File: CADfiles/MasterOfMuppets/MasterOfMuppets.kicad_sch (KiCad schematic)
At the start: 0 parts

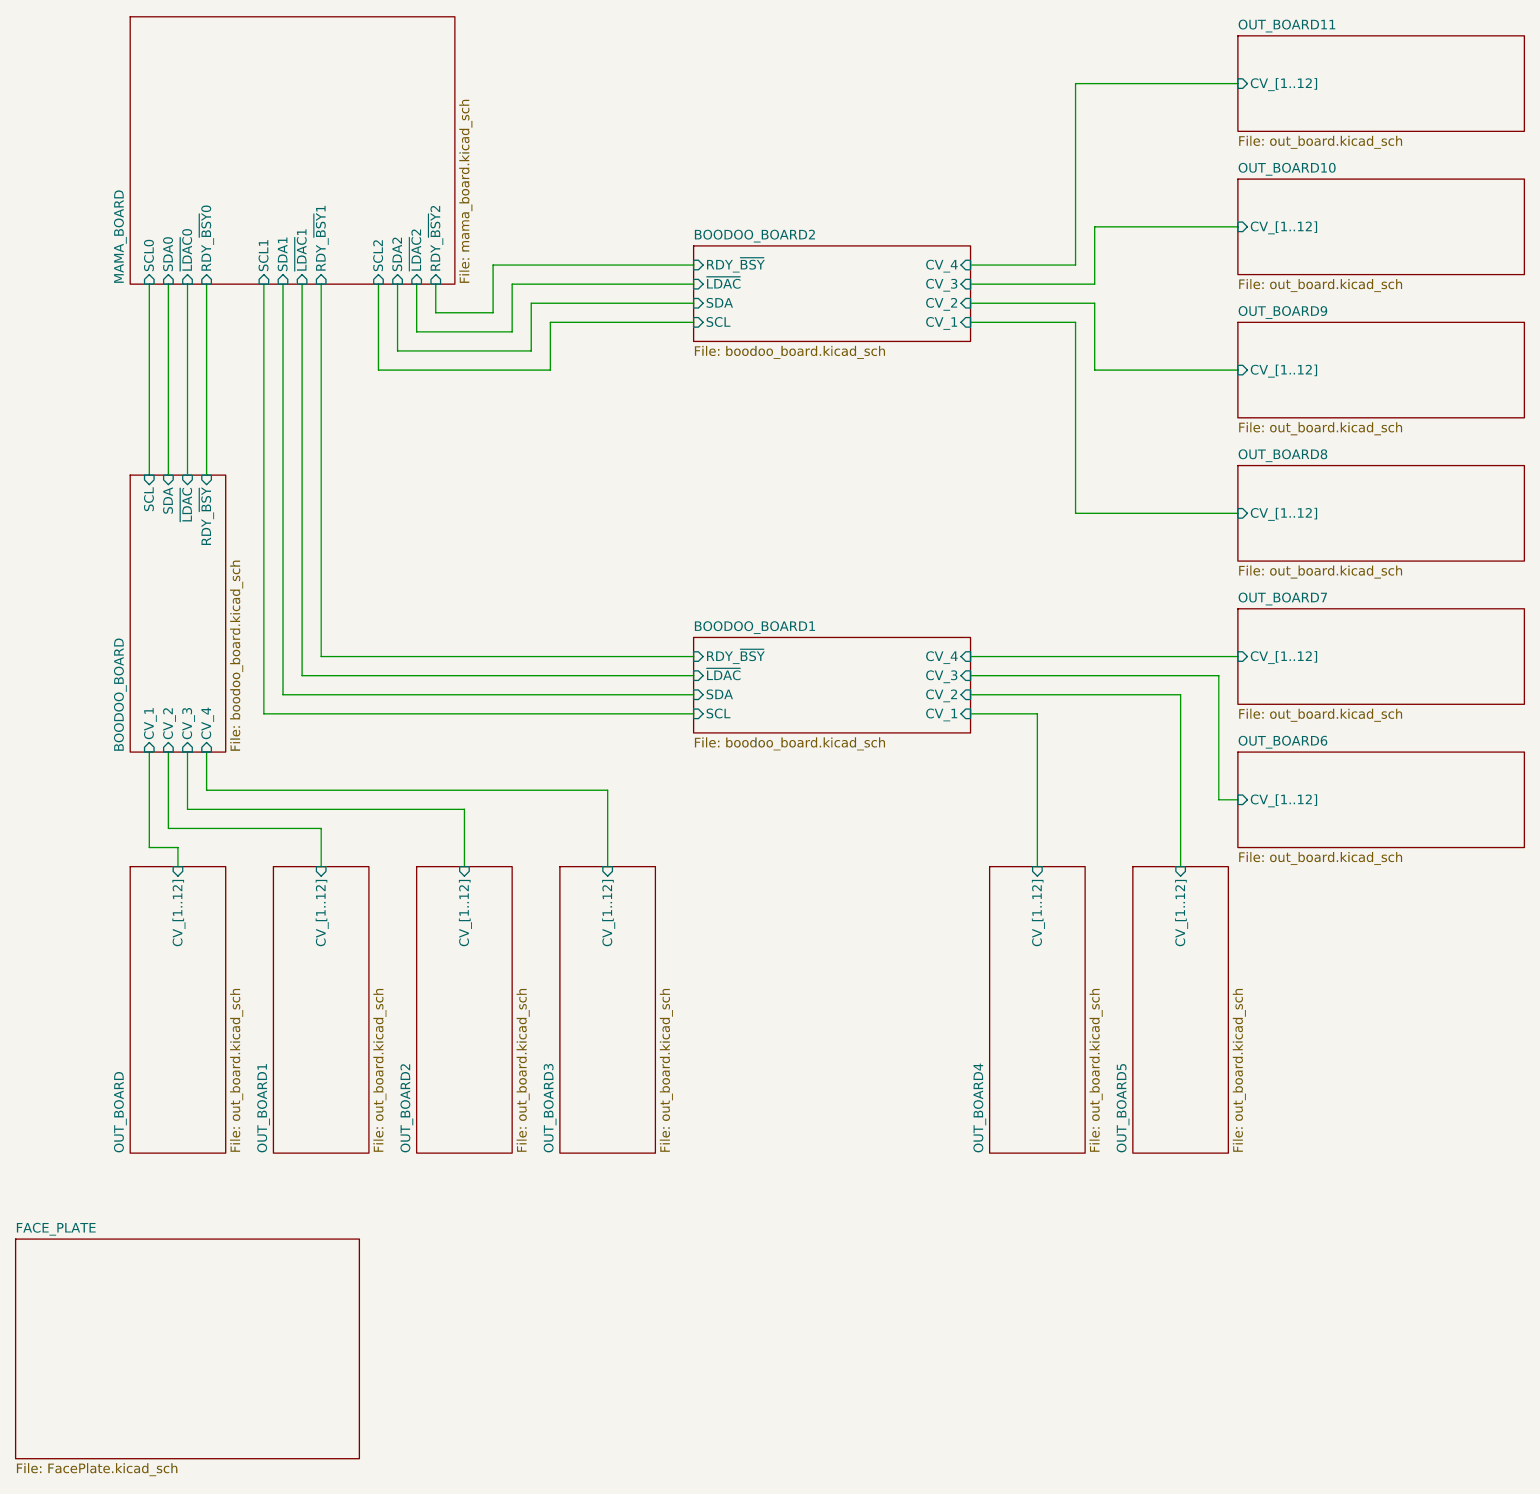
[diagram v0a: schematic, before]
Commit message: Refactoring schematics
Completely changed the schematics.
- Replaced MCP4728 with AD5593R;
- Added capacitors to reduce rippling everywhere;
- Adjusted the OpAmps that had a very bad configuration:
    - The TL074 had -Vcc on GND - it should be receiving -12V. This caused the OpAmp to spike when operating with low input voltages. In prototype it was replaced by LT1014D, which is about 5 times more expensive (although it is rail to rail out of the box and easy to setup);
    - Changed the feedback network isolation from 1k to 220Ohm, expecting have a more accurate feedback network;
    - Added a low pass filter between the DAC and the OpAmp (~1.6MHz - I might want to sync it with the USB package timing [1KHz]);
    - Using address bit to select the DAC, in case I decide to add multiple MIDI cables and make a monster with 32 outputs;
 - Renamed all sheets to make a bit more sense, and optimized all the schematic routing with sub packages. Probably PCB will follow,.
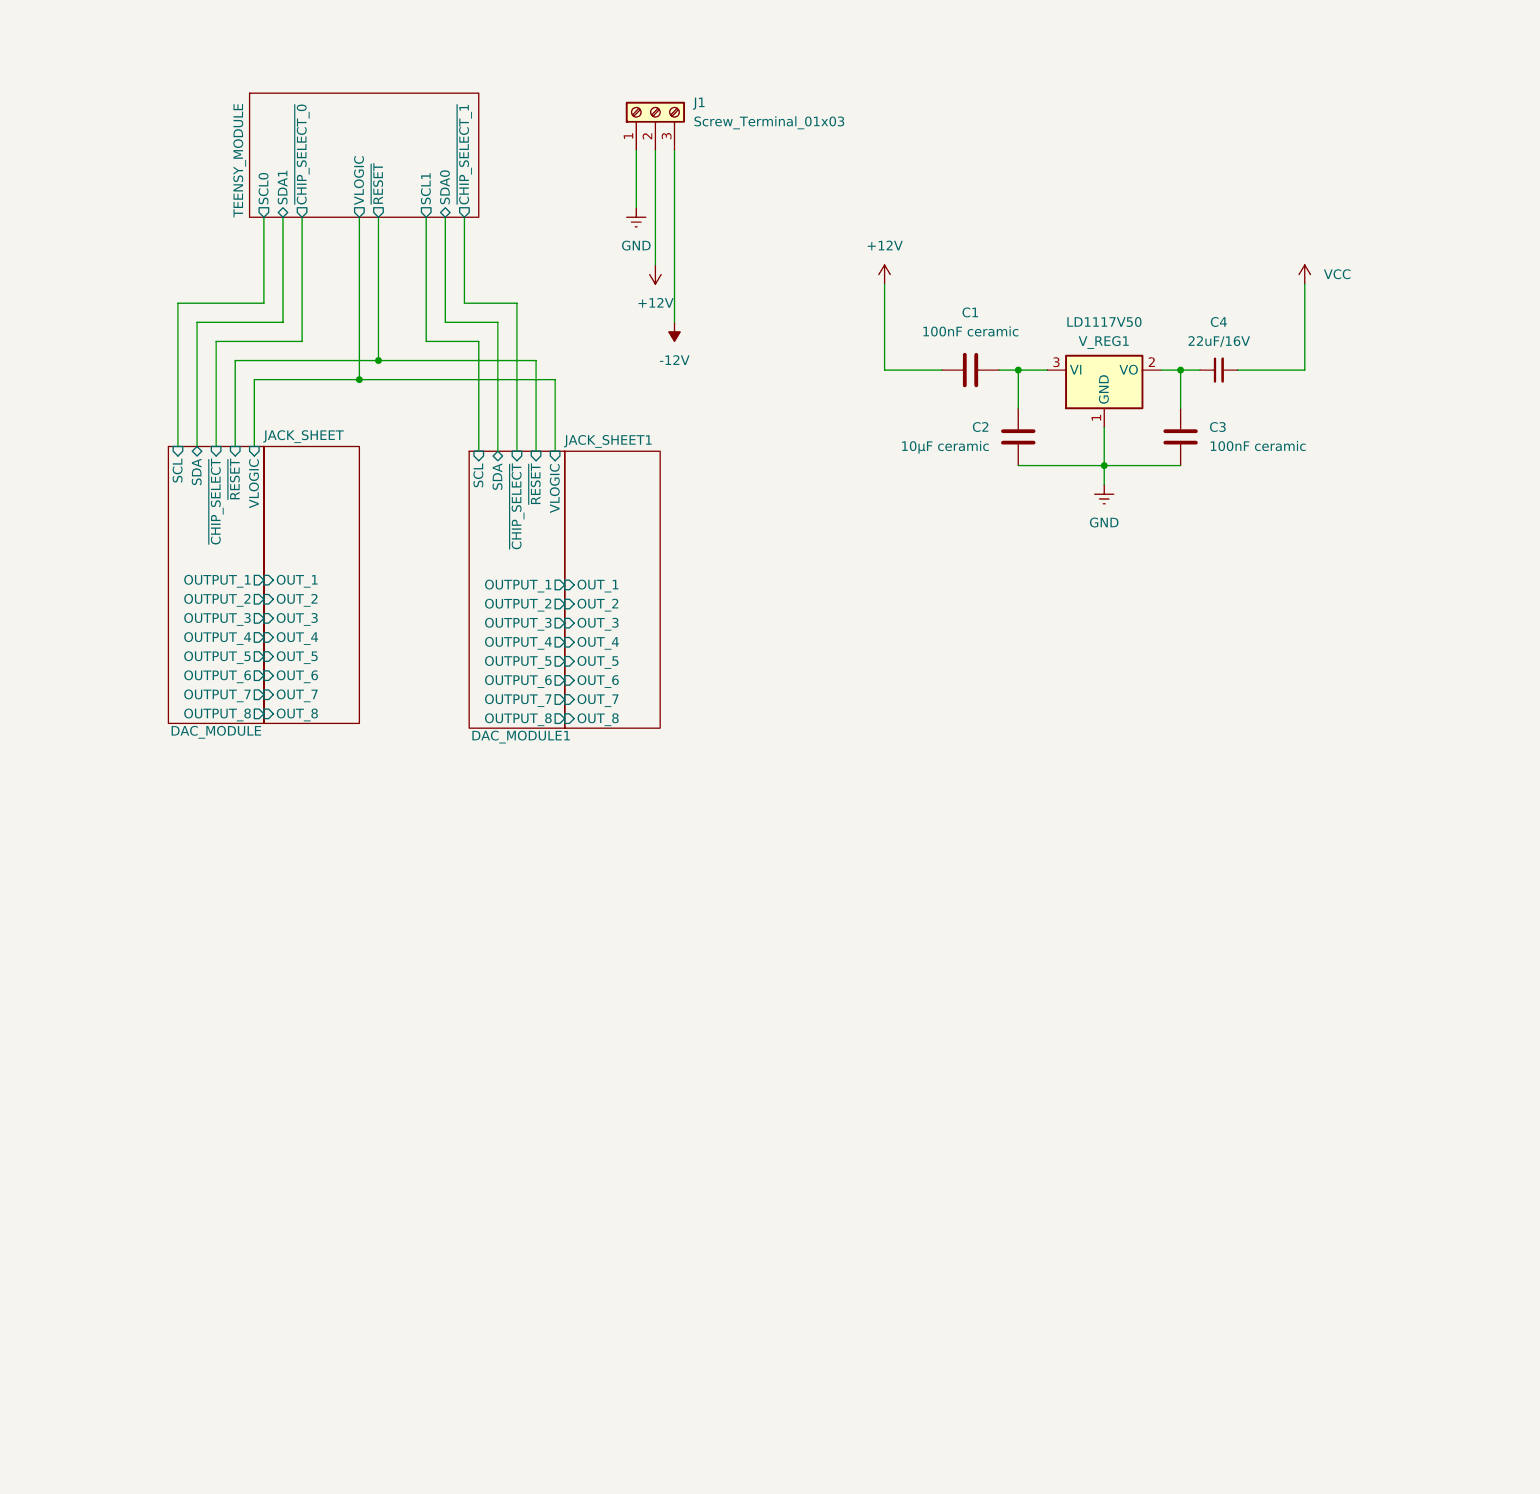
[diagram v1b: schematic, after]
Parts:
- added C1, C3: 100nF ceramic, symbol Device:C
- added C2: 10µF ceramic, symbol Device:C
- added C4: 22uF_0603_16V, 4ms_Capacitor:C_0805, symbol PCM_4ms_Capacitor:22uF_0603_16V
- added J1: Screw_Terminal_01x03, symbol Connector:Screw_Terminal_01x03
- added V_REG1: LD1117V50, PCM_4ms_Package_TO:TO-220-3_Vertical, symbol Regulator_Linear:LD1117S50TR_SOT223
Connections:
- new net: C1.2, C2.1, V_REG1.3 (VI)
- new net: C3.2, C4.1, V_REG1.2 (VO)
- new net +12V: C1.1, J1.2 (Pin_2)
- new net -12V: J1.3 (Pin_3)
- new net GND: C2.2, C3.1, J1.1 (Pin_1), V_REG1.1 (GND)
- new net VCC: C4.2
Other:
- sheet BOODOO_BOARD renamed DAC_MODULE
- sheet MAMA_BOARD renamed TEENSY_MODULE
- removed sheet BOODOO_BOARD1
- removed sheet BOODOO_BOARD2
- removed sheet FACE_PLATE
- removed sheet OUT_BOARD
- removed sheet OUT_BOARD1
- removed sheet OUT_BOARD10
- removed sheet OUT_BOARD11
- removed sheet OUT_BOARD2
- removed sheet OUT_BOARD3
- removed sheet OUT_BOARD4
- removed sheet OUT_BOARD5
- removed sheet OUT_BOARD6
- removed sheet OUT_BOARD7
- removed sheet OUT_BOARD8
- removed sheet OUT_BOARD9
- added sheet DAC_MODULE1 (dac_module.kicad_sch)
- added sheet JACK_SHEET (jack_sheet.kicad_sch)
- added sheet JACK_SHEET1 (jack_sheet.kicad_sch)
- sheet DAC_MODULE: file boodoo_board.kicad_sch -> dac_module.kicad_sch
- sheet DAC_MODULE ports: added OUTPUT_1, OUTPUT_2, OUTPUT_3, OUTPUT_4, OUTPUT_5, OUTPUT_6, OUTPUT_7, OUTPUT_8, VLOGIC, ~{CHIP_SELECT}, ~{RESET}; removed CV_1, CV_2, CV_3, CV_4, RDY_~{BSY}, ~{LDAC}
- sheet TEENSY_MODULE: file mama_board.kicad_sch -> teensy_module.kicad_sch
- sheet TEENSY_MODULE ports: added VLOGIC, ~{CHIP_SELECT_0}, ~{CHIP_SELECT_1}, ~{RESET}; removed RDY_~{BSY}0, RDY_~{BSY}1, RDY_~{BSY}2, SCL2, SDA2, ~{LDAC}0, ~{LDAC}1, ~{LDAC}2

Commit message: Preps for PCB Layout
- PCB Reset;
- Footprint assignment - opting for SMD over THT. I got tired of this much soldering;
- Fixing path for teensy.kicad_sym
- Changed symbols of the 3.5mm jack connector to the usual one seen in Eurorack (thanks for the symbols, 4ms!) ;
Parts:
- C1, C3: footprint (none) -> PCM_4ms_Capacitor:C_0603
- C2: footprint (none) -> PCM_4ms_Capacitor:C_0805
- J1: footprint (none) -> TerminalBlock:TerminalBlock_Xinya_XY308-2.54-3P_1x03_P2.54mm_Horizontal
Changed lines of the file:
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@@
 			)
 		)
-		(property "Footprint" ""
+		(property "Footprint" "TerminalBlock:TerminalBlock_Xinya_XY308-2.54-3P_1x03_P2.54mm_Horizontal"
 			(at 85.09 26.67 0)
 			(effects
@@
 			)
 		)
-		(property "Footprint" ""
+		(property "Footprint" "PCM_4ms_Capacitor:C_0603"
 			(at 130.81 59.9948 0)
 			(effects
@@
 			)
 		)
-		(property "Footprint" ""
+		(property "Footprint" "PCM_4ms_Capacitor:C_0603"
 			(at 153.9748 66.04 0)
 			(effects
@@
 			)
 		)
-		(property "Footprint" ""
+		(property "Footprint" "PCM_4ms_Capacitor:C_0805"
 			(at 132.3848 73.66 0)
 			(effects

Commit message: PCB Preps
Re-assigned footprints;
Placed all symbols in the middle;
Removed instruction to ignore the PCB in the README.manahmanah;
Added a generic placement recommendation file from Sir. Claude;
Ready to start the design;
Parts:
- C4: footprint 4ms_Capacitor:C_0805 -> PCM_4ms_Capacitor:C_0805
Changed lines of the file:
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@@
 			)
 		)
-		(property "Footprint" "4ms_Capacitor:C_0805"
+		(property "Footprint" "PCM_4ms_Capacitor:C_0805"
 			(at 165.1 63.5 0)
 			(effects

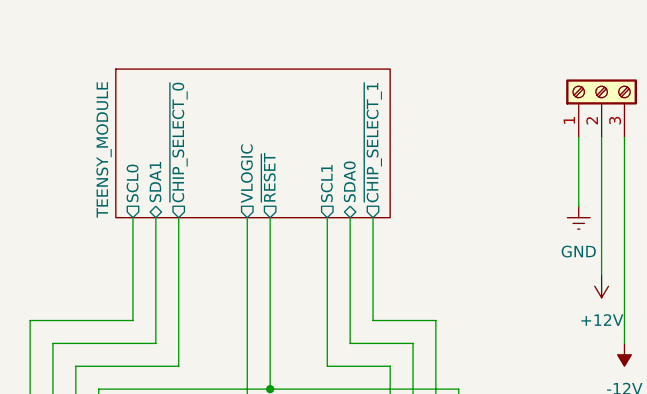
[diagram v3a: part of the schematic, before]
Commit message: Pin configuration
The current prototype board has DAC0 mapped to Wire2 and DAC1 mapped to Wire1. The schematics were updated to reflect it.
Added chip select in the firmware for AD5593R using the address pin as a selector.
Next steps: update Claude's knowledge about it.
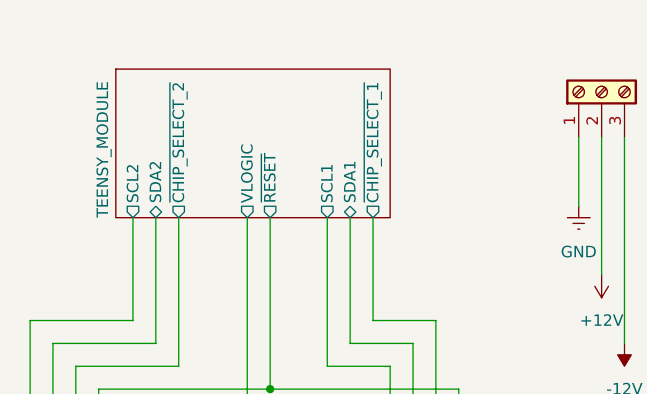
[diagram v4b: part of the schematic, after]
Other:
- sheet TEENSY_MODULE ports: added SCL2, SDA2, ~{CHIP_SELECT_2}; removed SCL0, SDA0, ~{CHIP_SELECT_0}
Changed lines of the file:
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@@
+	(wire
+		(pts
+			(xy 57.15 40.64) (xy 57.15 54.61)
+		)
+		(stroke
+			(width 0)
+			(type default)
+		)
+	)
 	(wire
 		(pts
@@
 	(wire
 		(pts
+			(xy 35.56 40.64) (xy 35.56 54.61)
+		)
+		(stroke
+			(width 0)
+			(type default)
+		)
+	)
+	(wire
+		(pts
 			(xy 48.26 40.64) (xy 48.26 59.69)
 		)
@@
 		(pts
 			(xy 33.02 40.64) (xy 33.02 52.07)
-		)
-		(stroke
-			(width 0)
-			(type default)
-		)
-	)
-	(wire
-		(pts
-			(xy 35.56 40.64) (xy 35.56 54.61)
-		)
-		(stroke
-			(width 0)
-			(type default)
-		)
-	)
-	(wire
-		(pts
-			(xy 57.15 40.64) (xy 57.15 54.61)
 		)
 		(stroke
@@
 			)
 		)
-		(pin "~{CHIP_SELECT_0}" output
-			(at 38.1 40.64 270)
-			(effects
-				(font
-					(size 1.27 1.27)
-				)
-				(justify left)
-			)
-		)
 		(pin "~{RESET}" output
 			(at 48.26 40.64 270)
@@
 		)
 		(pin "SDA1" bidirectional
-			(at 35.56 40.64 270)
-			(effects
-				(font
-					(size 1.27 1.27)
-				)
-				(justify left)
-			)
-		)
-		(pin "SCL0" output
-			(at 33.02 40.64 270)
+			(at 57.15 40.64 270)
 			(effects
 				(font
@@
 			)
 		)
-		(pin "SDA0" bidirectional
-			(at 57.15 40.64 270)
-			(effects
-				(font
+		(pin "SCL2" output
+			(at 33.02 40.64 270)
+			(effects
+				(font
+					(size 1.27 1.27)
+				)
+				(justify left)
+			)
+		)
+		(pin "SDA2" bidirectional
+			(at 35.56 40.64 270)
+			(effects
+				(font
+					(size 1.27 1.27)
+				)
+				(justify left)
+			)
+		)
+		(pin "~{CHIP_SELECT_2}" output
+			(at 38.1 40.64 270)
+			(effects
+				(font
